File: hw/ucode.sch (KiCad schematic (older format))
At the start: 16 parts, among them U501 74HC590, U502 74HCT02, U504 74HCT238, U505 74HCT238, U506 27C64, U507 27C64, U508 27C64, U509 74HCT175, U510 74HCT175, U511 74HCT175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

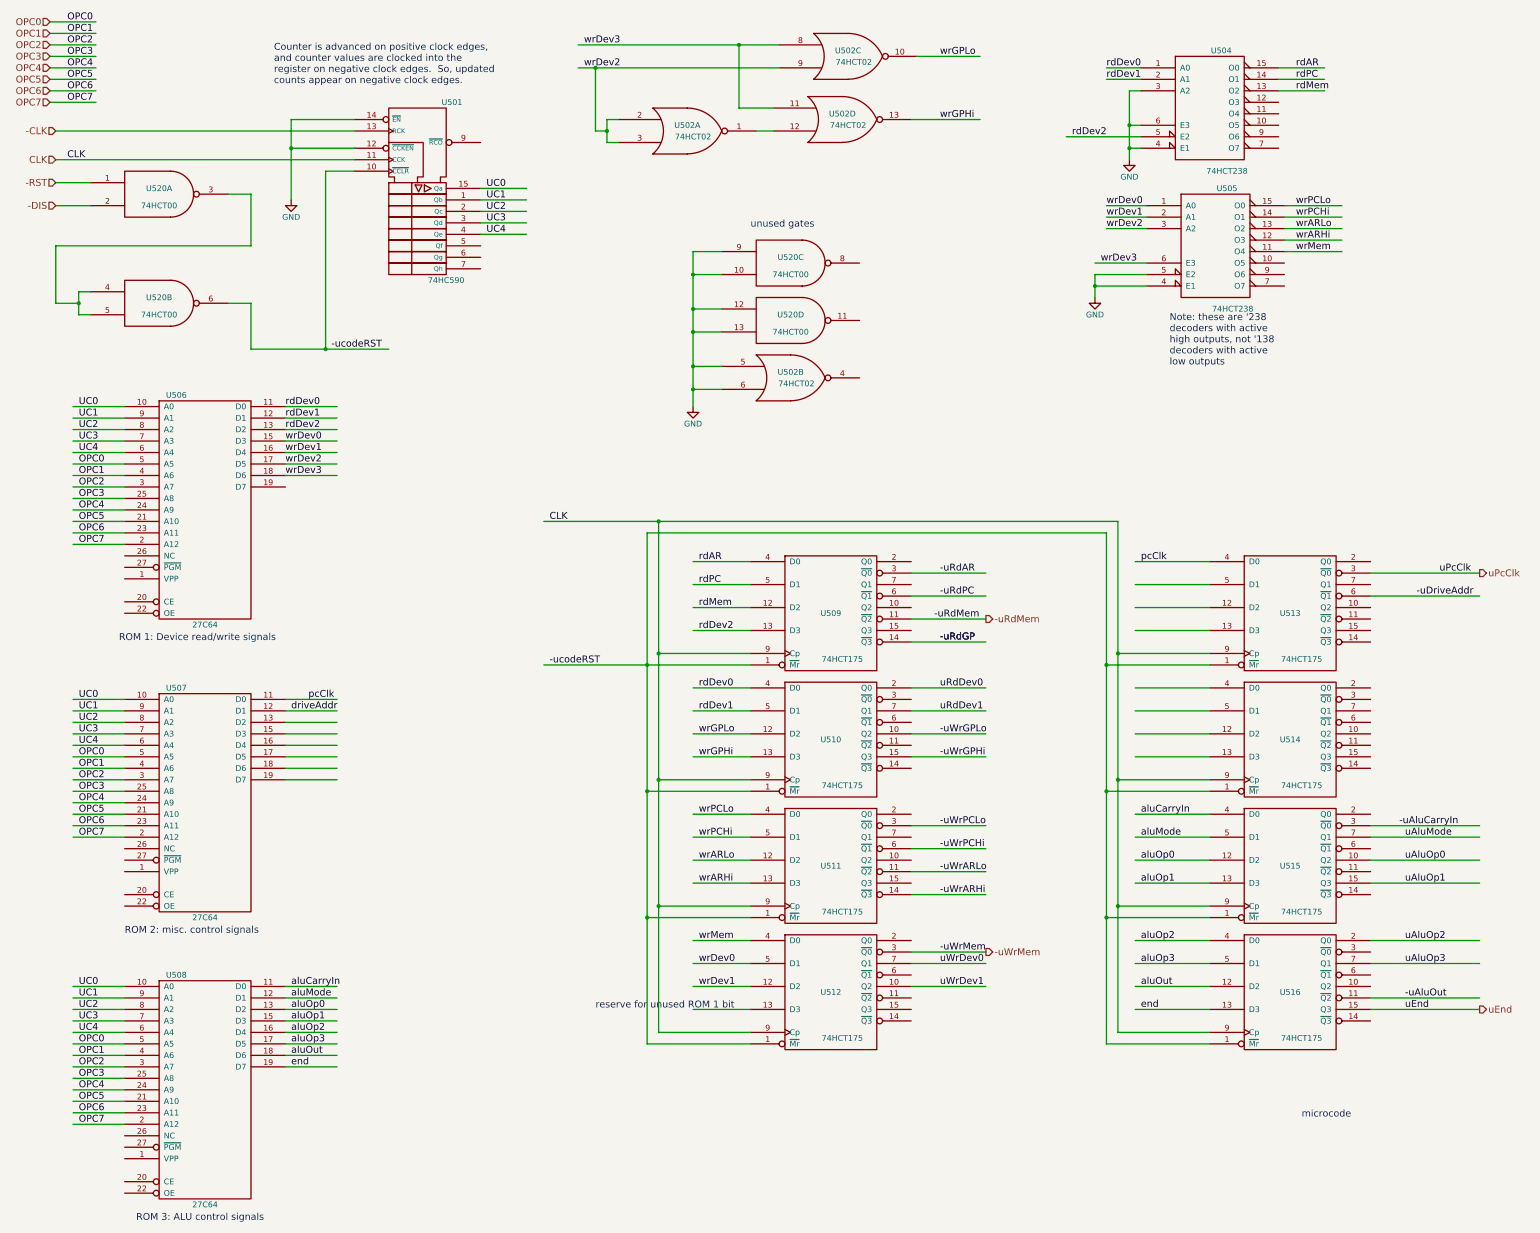
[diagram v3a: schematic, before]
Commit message: more fleshing out of microcode circuit
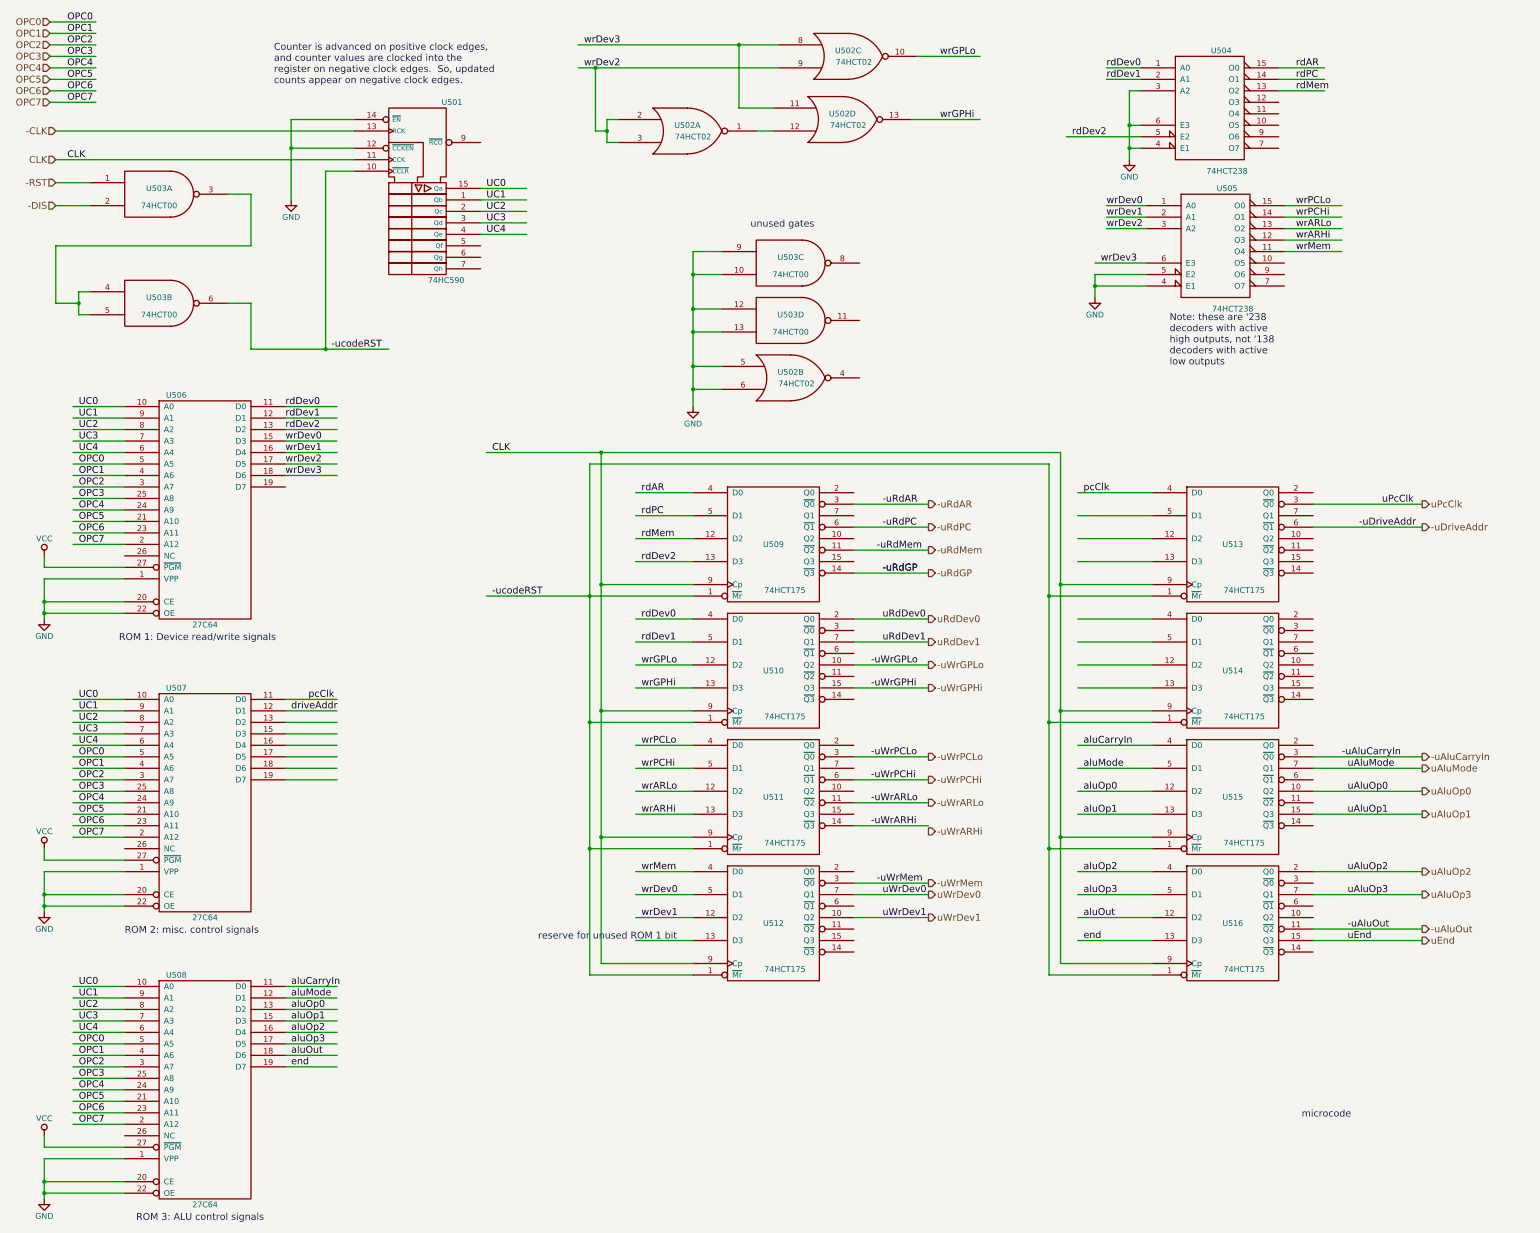
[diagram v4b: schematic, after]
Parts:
- renumbered U520 to U503
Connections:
- net labels added: VCC
- wire segments 215 -> 233
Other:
- moved on the sheet: U509, U510, U511, U512, U513, U514, U515, U516

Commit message: move end signal to first microcode ROM
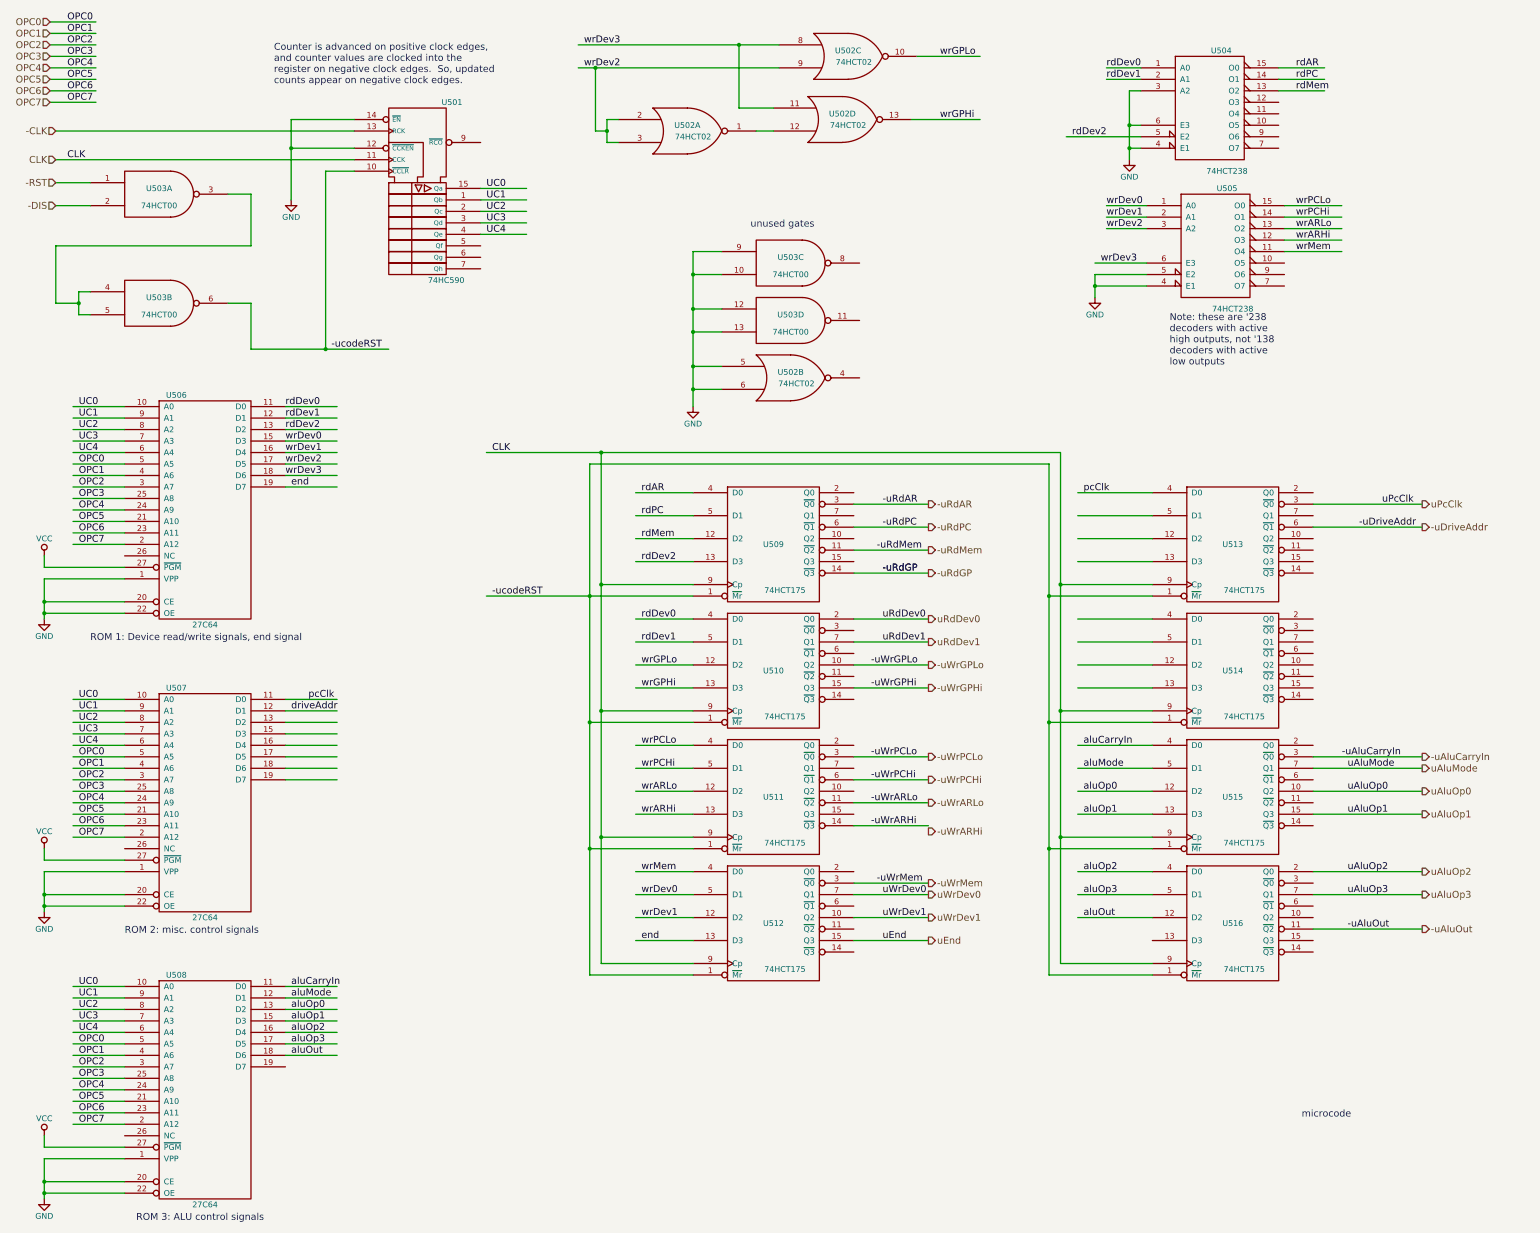
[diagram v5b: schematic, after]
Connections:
- wire segments 233 -> 266
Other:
- note added: "ROM 1: Device read/write signals, end signal"
- note removed: "ROM 1: Device read/write signals"
- note removed: "reserve for unused ROM 1 bit"
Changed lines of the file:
@@
 Text Label 8800 1500 0    60   ~ 0
 wrGPHi
-Text Notes 1650 6050 0    60   ~ 0
-ROM 1: Device read/write signals
+Text Notes 1400 6050 0    60   ~ 0
+ROM 1: Device read/write signals, end signal
 Text Label 10200 2750 0    60   ~ 0
 wrDev3
-Text Label 3150 9750 0    60   ~ 0
+Text Label 3150 4700 0    60   ~ 0
 end
 Text Label 3300 6550 0    60   ~ 0
@@
 Text HLabel 8700 8150 2    60   Output ~ 0
 -uWrMem
-Text HLabel 13000 8650 2    60   Output ~ 0
+Text HLabel 8700 8650 2    60   Output ~ 0
 uEnd
 Text HLabel 13000 4850 2    60   Output ~ 0
@@
 Text Label 8300 8450 0    60   ~ 0
 uWrDev1
-Text Notes 5300 8650 0    60   ~ 0
-reserve for unused ROM 1 bit
 Text Label 8300 5450 0    60   ~ 0
 -uRdGP
@@
 Text Label 12450 5050 0    60   ~ 0
 -uDriveAddr
-Text Label 10050 8650 0    60   ~ 0
+Text Label 6200 8650 0    60   ~ 0
 end
-Text Label 12350 8650 0    60   ~ 0
+Text Label 8300 8650 0    60   ~ 0
 uEnd
 Text Label 3150 9050 0    60   ~ 0
@@
 	10450 1750 10550 1750
 Wire Wire Line
-	10450 1250 10450 1850
+	10450 1250 10450 1550
+Wire Wire Line
+	10450 1550 10450 1750
+Wire Wire Line
+	10450 1750 10450 1850
 Wire Wire Line
 	10550 1050 10250 1050
@@
 	10600 2950 10150 2950
 Wire Wire Line
-	10150 2850 10150 3050
+	10150 2850 10150 2950
+Wire Wire Line
+	10150 2950 10150 3050
 Wire Wire Line
 	11800 2250 12300 2250
@@
 	11800 2650 12300 2650
 Wire Wire Line
-	5650 850  7400 850
-Wire Wire Line
-	5650 1050 7400 1050
+	5650 850  7050 850
+Wire Wire Line
+	7050 850  7400 850
+Wire Wire Line
+	5650 1050 5800 1050
+Wire Wire Line
+	5800 1050 7400 1050
 Wire Wire Line
 	8600 950  9150 950
@@
 	6000 1500 5900 1500
 Wire Wire Line
-	5900 1500 5900 1700
+	5900 1500 5900 1600
+Wire Wire Line
+	5900 1600 5900 1700
 Wire Wire Line
 	5900 1600 5800 1600
@@
 	10600 2750 10150 2750
 Wire Wire Line
-	3100 9750 3550 9750
+	3100 4700 3550 4700
 Wire Wire Line
 	3100 6550 3550 6550
@@
 	1400 3000 1300 3000
 Wire Wire Line
-	1300 3000 1300 3200
+	1300 3000 1300 3100
+Wire Wire Line
+	1300 3100 1300 3200
 Wire Wire Line
 	1300 3100 1100 3100
@@
 	2800 3100 2800 3500
 Wire Wire Line
-	2800 3500 4000 3500
-Wire Wire Line
-	4850 5650 6650 5650
+	2800 3500 3450 3500
+Wire Wire Line
+	3450 3500 4000 3500
+Wire Wire Line
+	4850 5650 5750 5650
+Wire Wire Line
+	5750 5650 6650 5650
 Wire Wire Line
 	5750 6750 6650 6750
 Wire Wire Line
-	5750 4500 5750 8950
+	5750 4500 5750 5650
+Wire Wire Line
+	5750 5650 5750 6750
+Wire Wire Line
+	5750 6750 5750 7850
+Wire Wire Line
+	5750 7850 5750 8950
 Connection ~ 5750 5650
 Wire Wire Line
@@
 	10650 5650 9750 5650
 Wire Wire Line
-	9750 4500 9750 8950
+	9750 4500 9750 5650
+Wire Wire Line
+	9750 5650 9750 6750
+Wire Wire Line
+	9750 6750 9750 7850
+Wire Wire Line
+	9750 7850 9750 8950
 Wire Wire Line
 	9750 4500 5750 4500
@@
 	6650 5550 5850 5550
 Wire Wire Line
-	5850 4400 5850 8850
-Wire Wire Line
-	4850 4400 9850 4400
+	5850 4400 5850 5550
+Wire Wire Line
+	5850 5550 5850 6650
+Wire Wire Line
+	5850 6650 5850 7750
+Wire Wire Line
+	5850 7750 5850 8850
+Wire Wire Line
+	4850 4400 5850 4400
+Wire Wire Line
+	5850 4400 9850 4400
 Wire Wire Line
 	5850 6650 6650 6650
@@
 	10650 5550 9850 5550
 Wire Wire Line
-	9850 4400 9850 8850
+	9850 4400 9850 5550
+Wire Wire Line
+	9850 5550 9850 6650
+Wire Wire Line
+	9850 6650 9850 7750
+Wire Wire Line
+	9850 7750 9850 8850
 Connection ~ 5850 4400
 Wire Wire Line
@@
 	3700 1750 3150 1750
 Wire Wire Line
-	3150 1500 3150 2200
+	3150 1500 3150 1750
+Wire Wire Line
+	3150 1750 3150 2200
 Wire Wire Line
 	3700 1500 3150 1500
@@
 	6900 2650 6650 2650
 Wire Wire Line
-	6650 2650 6650 4000
+	6650 2650 6650 2850
+Wire Wire Line
+	6650 2850 6650 3150
+Wire Wire Line
+	6650 3150 6650 3350
+Wire Wire Line
+	6650 3350 6650 3650
+Wire Wire Line
+	6650 3650 6650 3850
+Wire Wire Line
+	6650 3850 6650 4000
 Wire Wire Line
 	6900 2850 6650 2850
@@
 	6650 8450 6150 8450
 Wire Wire Line
-	6650 8650 6150 8650
-Wire Wire Line
 	8050 4850 8700 4850
 Wire Wire Line
@@
 	10650 8450 10000 8450
 Wire Wire Line
-	10650 8650 10000 8650
+	6650 8650 6150 8650
 Wire Wire Line
 	10650 8050 10000 8050
@@
 	12050 5050 13000 5050
 Wire Wire Line
-	12050 8650 13000 8650
+	8050 8650 8700 8650
 Wire Wire Line
 	3100 9050 3550 9050
@@
 	1700 5500 1000 5500
 Wire Wire Line
-	1000 5500 1000 5850
+	1000 5500 1000 5700
+Wire Wire Line
+	1000 5700 1000 5800
+Wire Wire Line
+	1000 5800 1000 5850
 Wire Wire Line
 	1700 5700 1000 5700
@@
 	1700 8050 1000 8050
 Wire Wire Line
-	1000 8050 1000 8400
+	1000 8050 1000 8250
+Wire Wire Line
+	1000 8250 1000 8350
+Wire Wire Line
+	1000 8350 1000 8400
 Wire Wire Line
 	1700 8250 1000 8250
@@
 	1700 10550 1000 10550
 Wire Wire Line
-	1000 10550 1000 10900
+	1000 10550 1000 10750
+Wire Wire Line
+	1000 10750 1000 10850
+Wire Wire Line
+	1000 10850 1000 10900
 Wire Wire Line
 	1700 10750 1000 10750

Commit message: microcode redesign
Rather than using logic to decode "packed" data
from the microcode, just use a 1:1 assignment of
microcode bits to control signals.  Since it looks
like 32 control signals will be sufficient, 4
microcode ROMs will do us.  Eliminating the
decoding logic reduces the chip count, and should
also result in better performance, since the
signals from the ROMs are clocked directly into
the '175 registers.
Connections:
- wire segments 266 -> 232
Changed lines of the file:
@@
 $Descr A3 16535 11693
 encoding utf-8
-Sheet 9 9
+Sheet 9 10
 Title ""
 Date ""
@@
 	10450 1750 10550 1750
 Wire Wire Line
-	10450 1250 10450 1550
-Wire Wire Line
-	10450 1550 10450 1750
-Wire Wire Line
-	10450 1750 10450 1850
+	10450 1250 10450 1850
 Wire Wire Line
 	10550 1050 10250 1050
@@
 	10600 2950 10150 2950
 Wire Wire Line
-	10150 2850 10150 2950
-Wire Wire Line
-	10150 2950 10150 3050
+	10150 2850 10150 3050
 Wire Wire Line
 	11800 2250 12300 2250
@@
 	11800 2650 12300 2650
 Wire Wire Line
-	5650 850  7050 850
-Wire Wire Line
-	7050 850  7400 850
-Wire Wire Line
-	5650 1050 5800 1050
-Wire Wire Line
-	5800 1050 7400 1050
+	5650 850  7400 850
+Wire Wire Line
+	5650 1050 7400 1050
 Wire Wire Line
 	8600 950  9150 950
@@
 	6000 1500 5900 1500
 Wire Wire Line
-	5900 1500 5900 1600
-Wire Wire Line
-	5900 1600 5900 1700
+	5900 1500 5900 1700
 Wire Wire Line
 	5900 1600 5800 1600
@@
 	1400 3000 1300 3000
 Wire Wire Line
-	1300 3000 1300 3100
-Wire Wire Line
-	1300 3100 1300 3200
+	1300 3000 1300 3200
 Wire Wire Line
 	1300 3100 1100 3100
@@
 	2800 3100 2800 3500
 Wire Wire Line
-	2800 3500 3450 3500
-Wire Wire Line
-	3450 3500 4000 3500
-Wire Wire Line
-	4850 5650 5750 5650
-Wire Wire Line
-	5750 5650 6650 5650
+	2800 3500 4000 3500
+Wire Wire Line
+	4850 5650 6650 5650
 Wire Wire Line
 	5750 6750 6650 6750
 Wire Wire Line
-	5750 4500 5750 5650
-Wire Wire Line
-	5750 5650 5750 6750
-Wire Wire Line
-	5750 6750 5750 7850
-Wire Wire Line
-	5750 7850 5750 8950
+	5750 4500 5750 8950
 Connection ~ 5750 5650
 Wire Wire Line
@@
 	10650 5650 9750 5650
 Wire Wire Line
-	9750 4500 9750 5650
-Wire Wire Line
-	9750 5650 9750 6750
-Wire Wire Line
-	9750 6750 9750 7850
-Wire Wire Line
-	9750 7850 9750 8950
+	9750 4500 9750 8950
 Wire Wire Line
 	9750 4500 5750 4500
@@
 	6650 5550 5850 5550
 Wire Wire Line
-	5850 4400 5850 5550
-Wire Wire Line
-	5850 5550 5850 6650
-Wire Wire Line
-	5850 6650 5850 7750
-Wire Wire Line
-	5850 7750 5850 8850
-Wire Wire Line
-	4850 4400 5850 4400
-Wire Wire Line
-	5850 4400 9850 4400
+	5850 4400 5850 8850
+Wire Wire Line
+	4850 4400 9850 4400
 Wire Wire Line
 	5850 6650 6650 6650
@@
 	10650 5550 9850 5550
 Wire Wire Line
-	9850 4400 9850 5550
-Wire Wire Line
-	9850 5550 9850 6650
-Wire Wire Line
-	9850 6650 9850 7750
-Wire Wire Line
-	9850 7750 9850 8850
+	9850 4400 9850 8850
 Connection ~ 5850 4400
 Wire Wire Line
@@
 	3700 1750 3150 1750
 Wire Wire Line
-	3150 1500 3150 1750
-Wire Wire Line
-	3150 1750 3150 2200
+	3150 1500 3150 2200
 Wire Wire Line
 	3700 1500 3150 1500
@@
 	6900 2650 6650 2650
 Wire Wire Line
-	6650 2650 6650 2850
-Wire Wire Line
-	6650 2850 6650 3150
-Wire Wire Line
-	6650 3150 6650 3350
-Wire Wire Line
-	6650 3350 6650 3650
-Wire Wire Line
-	6650 3650 6650 3850
-Wire Wire Line
-	6650 3850 6650 4000
+	6650 2650 6650 4000
 Wire Wire Line
 	6900 2850 6650 2850
@@
 	1700 5500 1000 5500
 Wire Wire Line
-	1000 5500 1000 5700
-Wire Wire Line
-	1000 5700 1000 5800
-Wire Wire Line
-	1000 5800 1000 5850
+	1000 5500 1000 5850
 Wire Wire Line
 	1700 5700 1000 5700
@@
 	1700 8050 1000 8050
 Wire Wire Line
-	1000 8050 1000 8250
-Wire Wire Line
-	1000 8250 1000 8350
-Wire Wire Line
-	1000 8350 1000 8400
+	1000 8050 1000 8400
 Wire Wire Line
 	1700 8250 1000 8250
@@
 	1700 10550 1000 10550
 Wire Wire Line
-	1000 10550 1000 10750
-Wire Wire Line
-	1000 10750 1000 10850
-Wire Wire Line
-	1000 10850 1000 10900
+	1000 10550 1000 10900
 Wire Wire Line
 	1700 10750 1000 10750
